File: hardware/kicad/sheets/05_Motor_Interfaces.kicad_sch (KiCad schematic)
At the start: 47 parts, among them U1 SN74LVC-Q1: R_OK = RPWM AND N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, U2 SN74LVC-Q1: R_OK = RPWM AND N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, U3 SN74LVC-Q1: EN = PERMIT AND N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, U4 SN74LXC4T245-class Axis 1; A→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, U5 SN74LXC4T245-class Axis 2; A→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

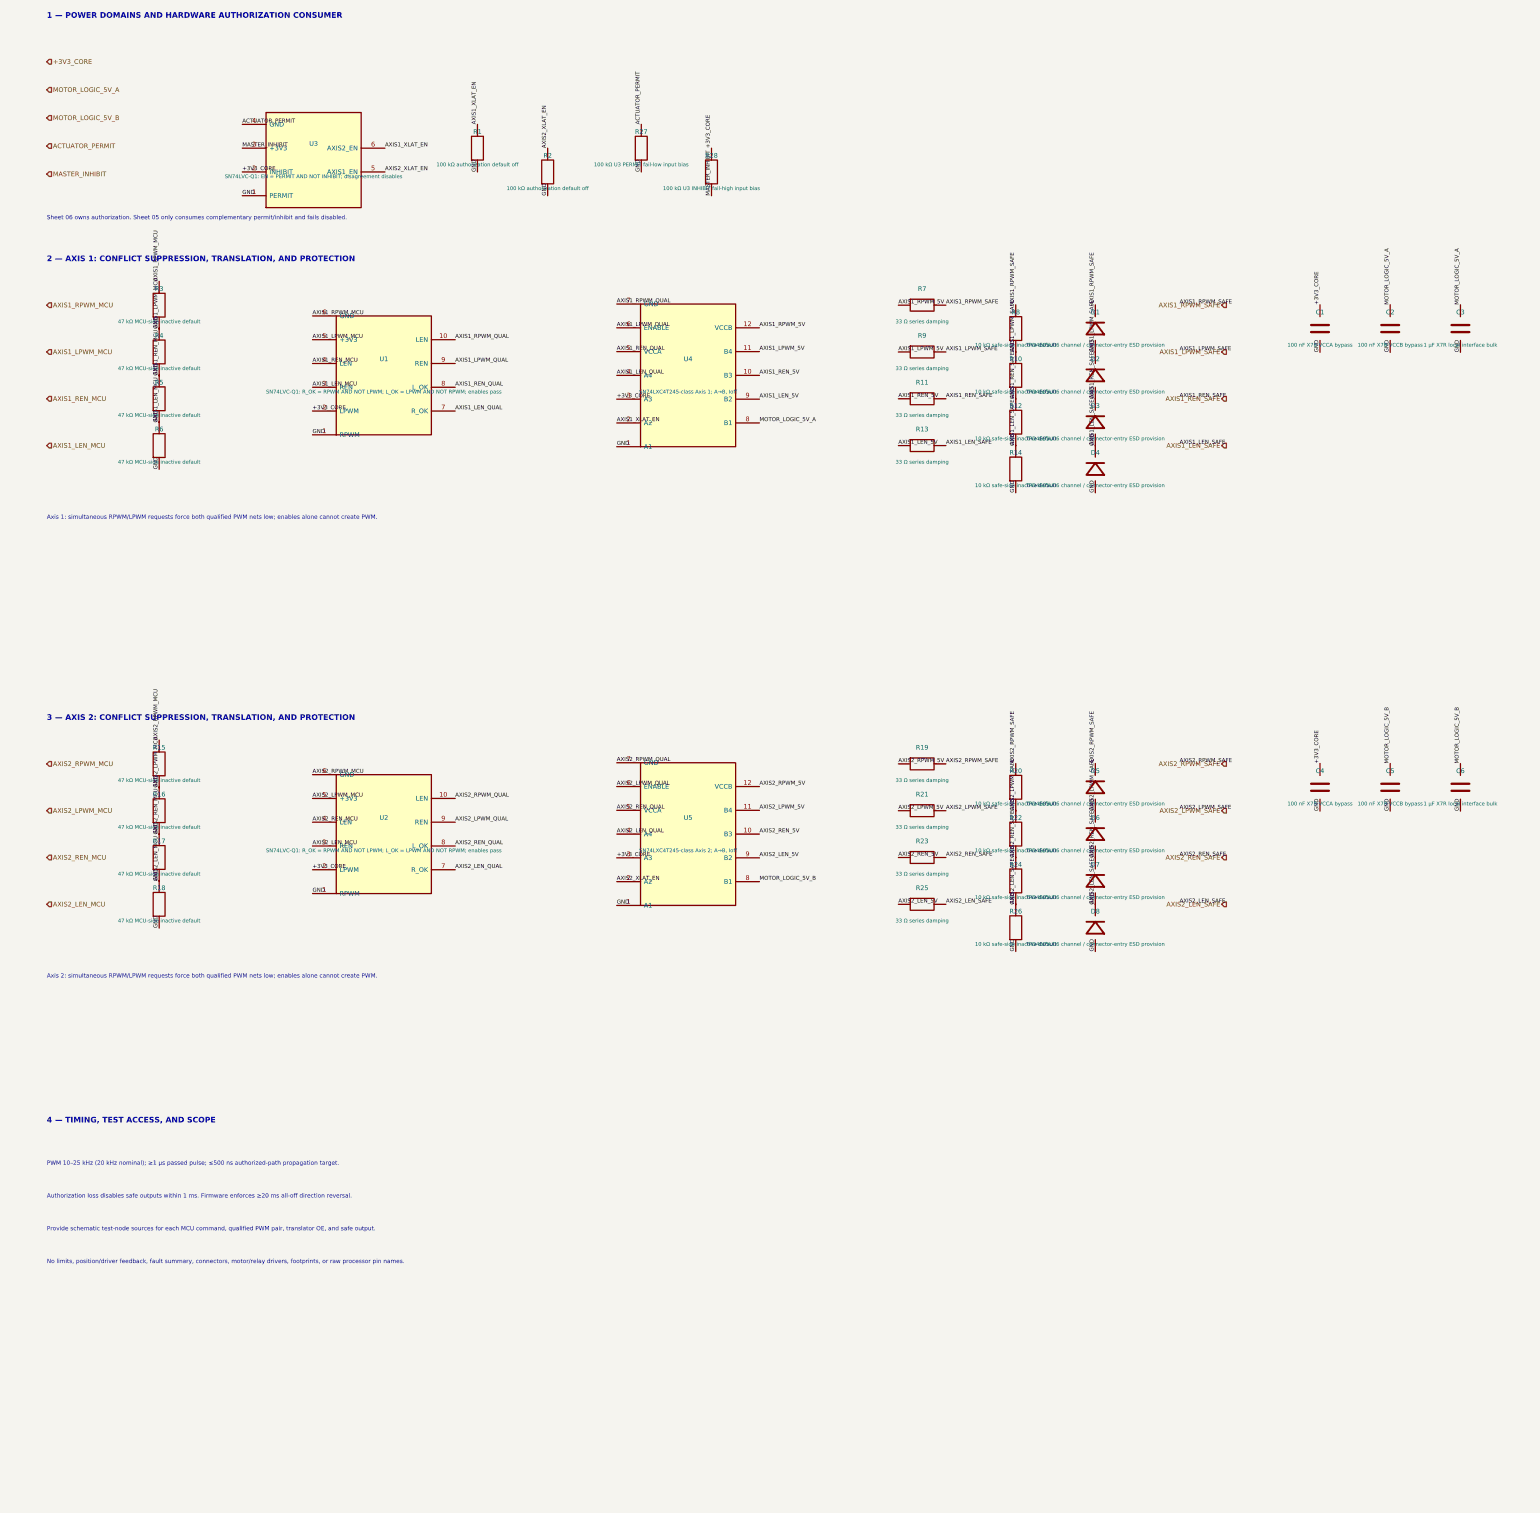
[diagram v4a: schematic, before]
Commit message: Normalize Rev A reference designators
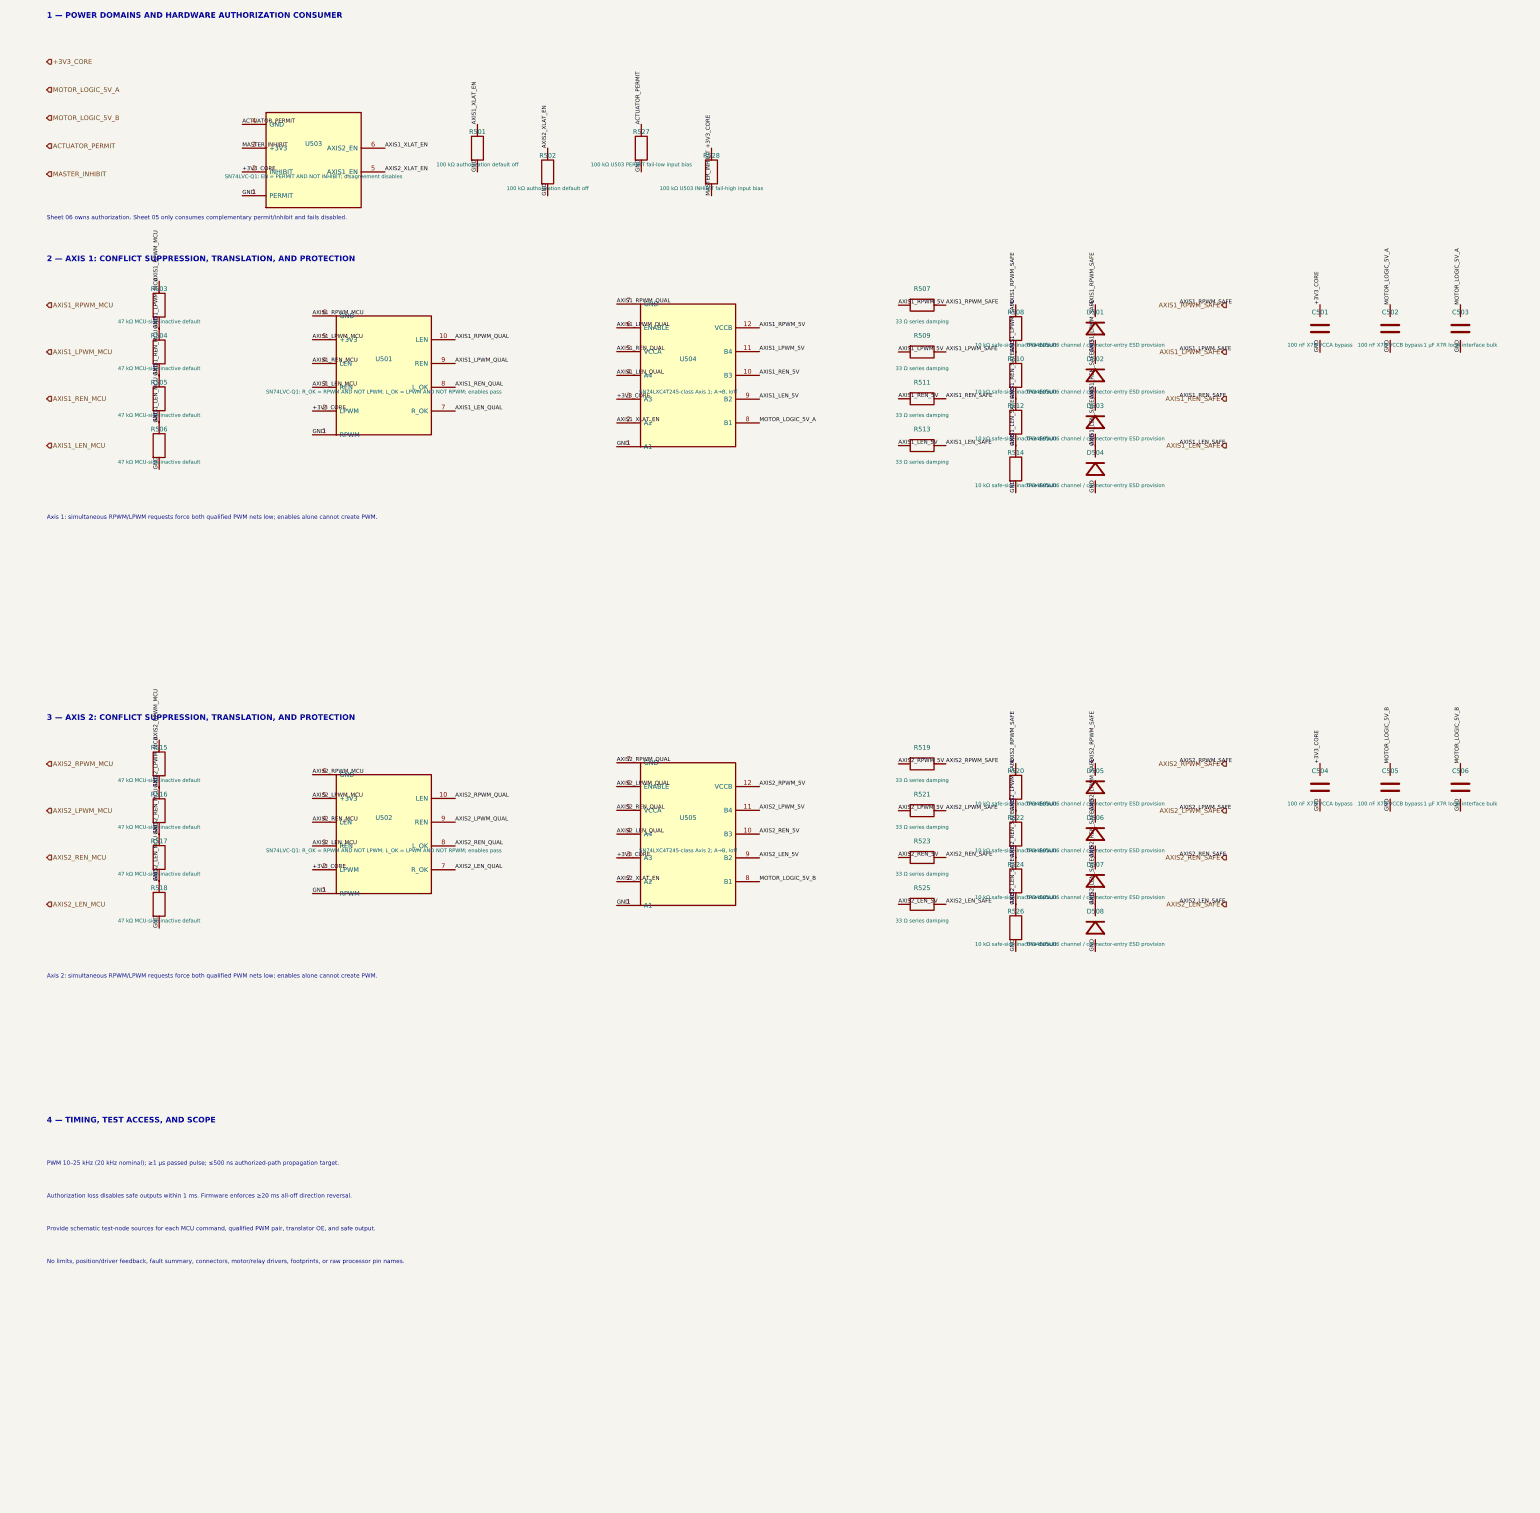
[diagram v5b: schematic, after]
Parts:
- R527: renamed from R27; value 100 kΩ U3 PERMIT fail-low input bias -> 100 kΩ U503 PERMIT fail-low input bias
- R528: renamed from R28; value 100 kΩ U3 INHIBIT fail-high input bias -> 100 kΩ U503 INHIBIT fail-high input bias
- renumbered C1 to C501, C2 to C502, C3 to C503, C4 to C504, C5 to C505, C6 to C506, D1 to D501, D2 to D502, D3 to D503, D4 to D504, D5 to D505, D6 to D506, D7 to D507, D8 to D508, R1 to R501, R2 to R502, R3 to R503, R4 to R504, R5 to R505, R6 to R506, R7 to R507, R8 to R508, R9 to R509, R10 to R510, R11 to R511, R12 to R512, R13 to R513, R14 to R514, R15 to R515, R16 to R516, R17 to R517, R18 to R518, R19 to R519, R20 to R520, R21 to R521, R22 to R522, R23 to R523, R24 to R524, R25 to R525, R26 to R526, U1 to U501, U2 to U502, U3 to U503, U4 to U504, U5 to U505

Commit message: Physically decompose Sheet 05 motion logic
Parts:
- removed U501, U502: SN74LVC-Q1: R_OK = RPWM AND NOT LPWM; L_OK = LPWM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, symbol IPC100:INTERLOCK4
- removed U503: SN74LVC-Q1: EN = PERMIT AND NOT INHIBIT; disagree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, symbol IPC100:AUTH2
- added C507: 100 nF X7R U506 package-local bypass, symbol IPC100:C
- added C508: 100 nF X7R U507 package-local bypass, symbol IPC100:C
- added C509: 100 nF X7R U508 package-local bypass, symbol IPC100:C
- added TP501: AXIS1_RPWM_MCU, symbol IPC100:TP
- added TP502: AXIS1_LPWM_MCU, symbol IPC100:TP
- added TP503: AXIS1_RPWM_QUAL, symbol IPC100:TP
- added TP504: AXIS1_LPWM_QUAL, symbol IPC100:TP
- added TP505: AXIS1_XLAT_EN, symbol IPC100:TP
- added TP506: AXIS1_RPWM_5V, symbol IPC100:TP
- added TP507: AXIS1_LPWM_5V, symbol IPC100:TP
- added TP508: AXIS1_RPWM_SAFE, symbol IPC100:TP
- added TP509: AXIS1_LPWM_SAFE, symbol IPC100:TP
- added TP510: AXIS1_REN_SAFE, symbol IPC100:TP
- added TP511: AXIS1_LEN_SAFE, symbol IPC100:TP
- added TP512: AXIS2_RPWM_MCU, symbol IPC100:TP
- added TP513: AXIS2_LPWM_MCU, symbol IPC100:TP
- added TP514: AXIS2_RPWM_QUAL, symbol IPC100:TP
- added TP515: AXIS2_LPWM_QUAL, symbol IPC100:TP
- added TP516: AXIS2_XLAT_EN, symbol IPC100:TP
- added TP517: AXIS2_RPWM_5V, symbol IPC100:TP
- added TP518: AXIS2_LPWM_5V, symbol IPC100:TP
- added TP519: AXIS2_RPWM_SAFE, symbol IPC100:TP
- added TP520: AXIS2_LPWM_SAFE, symbol IPC100:TP
- added TP521: AXIS2_REN_SAFE, symbol IPC100:TP
- added TP522: AXIS2_LEN_SAFE, symbol IPC100:TP
- added TP523: ACTUATOR_PERMIT, symbol IPC100:TP
- added TP524: MASTER_INHIBIT, symbol IPC100:TP
- added U506: SN74LVC14AQPWRQ1, symbol IPC100:SN74LVC14AQPWRQ1
- added U507, U508: SN74LVC08AQPWRQ1, symbol IPC100:SN74LVC08AQPWRQ1
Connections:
- net +3V3_CORE: no longer C501.2, C504.2, R528.2, U504.3 (A3), U505.3 (A3)
- net ACTUATOR_PERMIT: no longer R527.2
- net AXIS1_LEN_5V: no longer R513.1, U504.9 (B2)
- net AXIS1_LEN_MCU: no longer R506.2
- net AXIS1_LEN_SAFE: no longer D504.2, R513.2, R514.2
- net AXIS1_LPWM_5V: no longer R509.1, U504.11 (B4)
- net AXIS1_LPWM_MCU: no longer R504.2
- net AXIS1_LPWM_QUAL: no longer U504.6 (ENABLE)
- net AXIS1_LPWM_SAFE: no longer D502.2, R509.2, R510.2
- net AXIS1_REN_5V: no longer R511.1, U504.10 (B3)
- net AXIS1_REN_MCU: no longer R505.2
- net AXIS1_REN_SAFE: no longer D503.2, R511.2, R512.2
- net AXIS1_RPWM_5V: no longer R507.1, U504.12 (VCCB)
- net AXIS1_RPWM_MCU: no longer R503.2
- net AXIS1_RPWM_QUAL: no longer U504.7 (GND)
- net AXIS1_RPWM_SAFE: no longer D501.2, R507.2, R508.2
- net AXIS1_XLAT_EN: no longer R501.2, U504.2 (A2)
- net AXIS2_LEN_5V: no longer R525.1, U505.9 (B2)
- net AXIS2_LEN_MCU: no longer R518.2
- net AXIS2_LEN_SAFE: no longer D508.2, R525.2, R526.2
- net AXIS2_LPWM_5V: no longer R521.1, U505.11 (B4)
- net AXIS2_LPWM_MCU: no longer R516.2
- net AXIS2_LPWM_QUAL: no longer U505.6 (ENABLE)
- net AXIS2_LPWM_SAFE: no longer D506.2, R521.2, R522.2
- net AXIS2_REN_5V: no longer R523.1, U505.10 (B3)
- net AXIS2_REN_MCU: no longer R517.2
- net AXIS2_REN_SAFE: no longer D507.2, R523.2, R524.2
- net AXIS2_RPWM_5V: no longer R519.1, U505.12 (VCCB)
- net AXIS2_RPWM_MCU: no longer R515.2
- net AXIS2_RPWM_QUAL: no longer U505.7 (GND)
- net AXIS2_RPWM_SAFE: no longer D505.2, R519.2, R520.2
- net AXIS2_XLAT_EN: no longer R502.2, U505.2 (A2)
- net GND: no longer C501.1, C502.1, C503.1, C504.1, C505.1, C506.1, D501.1, D502.1, D503.1, D504.1, D505.1, D506.1, D507.1, D508.1, R501.1, R502.1, R503.1, R504.1, R505.1, R506.1, R508.1, R510.1, R512.1, R514.1, R515.1, R516.1, R517.1, R518.1, R520.1, R522.1, R524.1, R526.1, R527.1, U504.1 (A1), U505.1 (A1)
- net MASTER_INHIBIT: no longer R528.1
- net MOTOR_LOGIC_5V_A: no longer C502.2, C503.2, U504.8 (B1)
- net MOTOR_LOGIC_5V_B: no longer C505.2, C506.2, U505.8 (B1)
- removed net AXIS1_LEN_QUAL: U504.4 (A4)
- removed net AXIS1_REN_QUAL: U504.5 (VCCA)
- removed net AXIS2_LEN_QUAL: U505.4 (A4)
- removed net AXIS2_REN_QUAL: U505.5 (VCCA)
- no-connect marks 0 -> 3
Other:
- note added: "ECO-011A2 â€” PHYSICAL SUPPRESSION AND AUTHORIZATION LOGIC"
- note added: "R_OK = RPWM AND NOT LPWM; L_OK = LPWM AND NOT RPWM; EN = PERMIT AND NOT INHIBIT; AXISn_XLAT_EN = ACTUATOR_PERMIT AND NOT MASTER_INHIBIT"
